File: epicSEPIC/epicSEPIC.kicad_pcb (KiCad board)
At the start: 2 copper layers, 24 x 27.4 mm, 12 parts, among them J1 Screw_Terminal_01x02, J2 Screw_Terminal_01x02, Q1 ISZ230N10NM6, U1 1EDN7550U

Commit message: PCB prototipo mejorado
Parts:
- added C4: 0.22u, Capacitor_SMD:C_0603_1608Metric, B.Cu at (165.0, 129.8)
- added C5: 0.1u, Capacitor_SMD:C_0603_1608Metric, B.Cu at (165.0, 126.3)
- added U2: LM7815, Package_TO_SOT_SMD:SOT-223-3_TabPin2, B.Cu at (171.0, 128.0)
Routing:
- net input: track 0.00 -> 17.4 mm, vias 0 -> 4
- net /S_Diodo: track 4.34 -> 0.00 mm
- net VDD: track 0.00 -> 2.93 mm, vias 0 -> 3
- added copper zone on F.Cu, net /S_Diodo
- added copper zone on B.Cu, net VDD
- added copper zone on F.Cu, net VDD
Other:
- board size 24 x 27.4 mm -> 28 x 28 mm

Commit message: PCB Final en proceso, encontré el inductor
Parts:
- added L1: 1.8m, footprints:SRF1280680M, F.Cu at (183.5, 113.2)
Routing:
- added copper zone on B.Cu, net input
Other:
- board outline removed

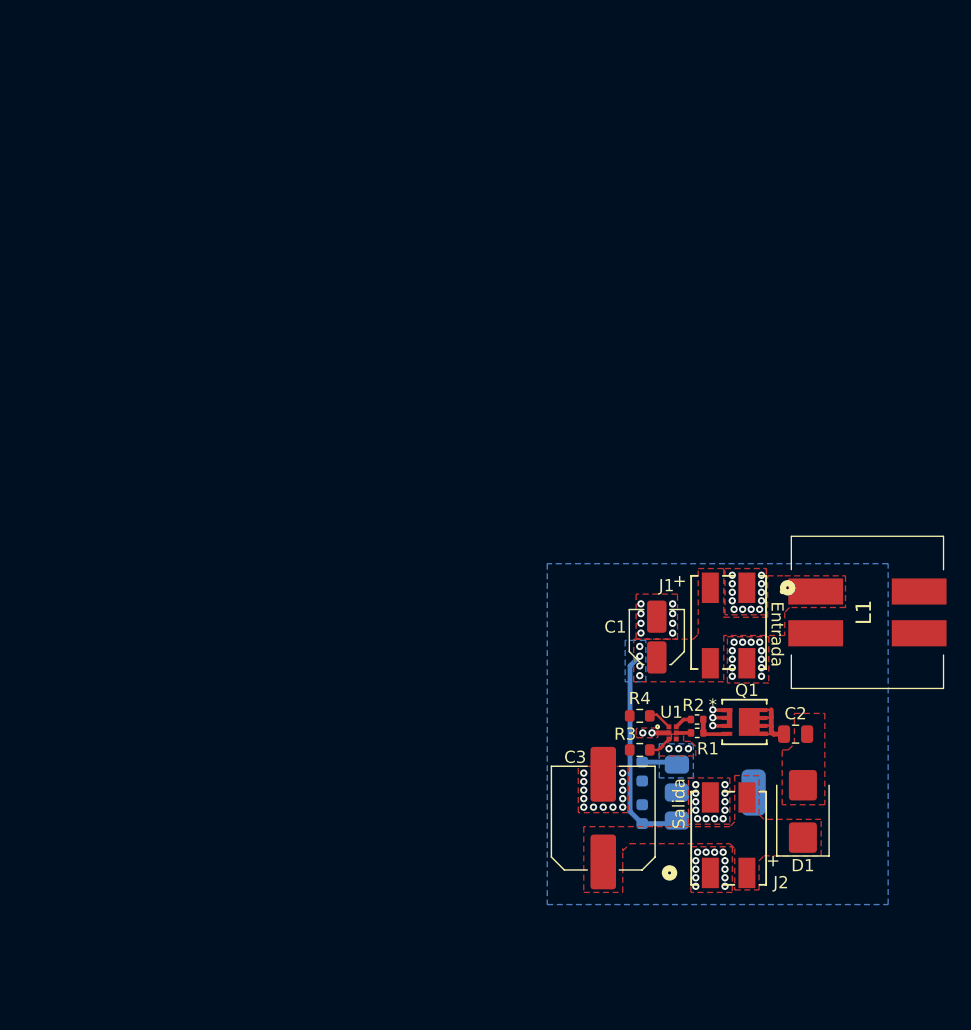
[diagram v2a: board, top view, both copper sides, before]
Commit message: Agregar repo submodulo para informe
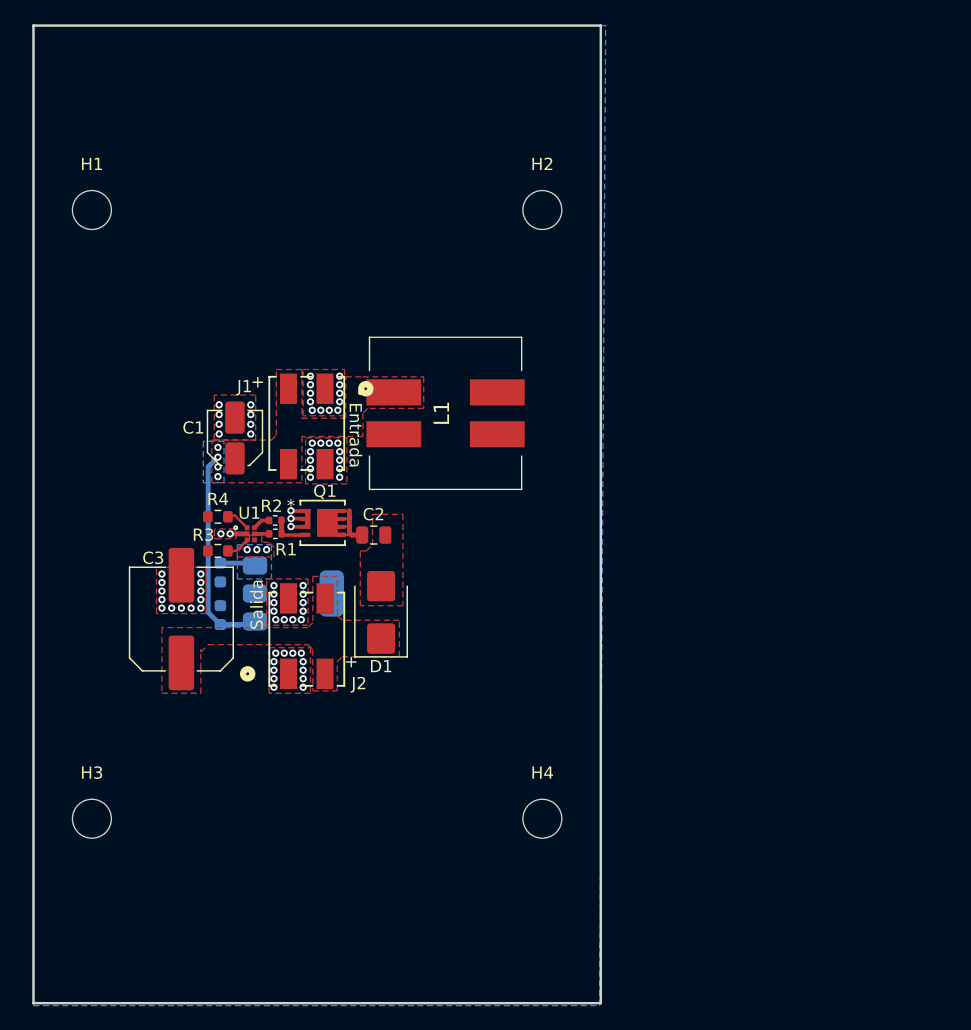
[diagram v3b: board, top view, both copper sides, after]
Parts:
- added H1: MountingHole, MountingHole:MountingHole_3.2mm_M3_ISO14580, F.Cu at (119.8, 80.2)
- added H2: MountingHole, MountingHole:MountingHole_3.2mm_M3_ISO14580, F.Cu at (156.8, 80.2)
- added H3: MountingHole, MountingHole:MountingHole_3.2mm_M3_ISO14580, F.Cu at (119.8, 130.2)
- added H4: MountingHole, MountingHole:MountingHole_3.2mm_M3_ISO14580, F.Cu at (156.8, 130.2)
- moved C2 38.3 mm to (142.9, 106.8)
- moved C4 38.3 mm to (130.3, 113.4)
- moved C5 38.3 mm to (130.3, 109.9)
- moved J1 38.3 mm to (137.4, 97.7)
- moved L1 38.3 mm to (148.8, 96.8)
- moved Q1 38.3 mm to (138.8, 105.8)
- moved R1 38.3 mm to (134.9, 106.8)
- moved R4 38.3 mm to (130.2, 105.3)
- moved U1 38.3 mm to (132.8, 106.8)
- moved C3 38.3 mm to (127.2, 113.8)
- moved J2 38.3 mm to (137.5, 115.4)
- moved R3 38.3 mm to (130.2, 108.2)
- moved U2 38.3 mm to (136.3, 111.7)
- moved D1 38.3 mm to (143.6, 113.2)
- moved C1 38.3 mm to (131.6, 98.9)
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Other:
- board outline added: 46.6 x 80.3 mm

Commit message: Diseño de PCB final
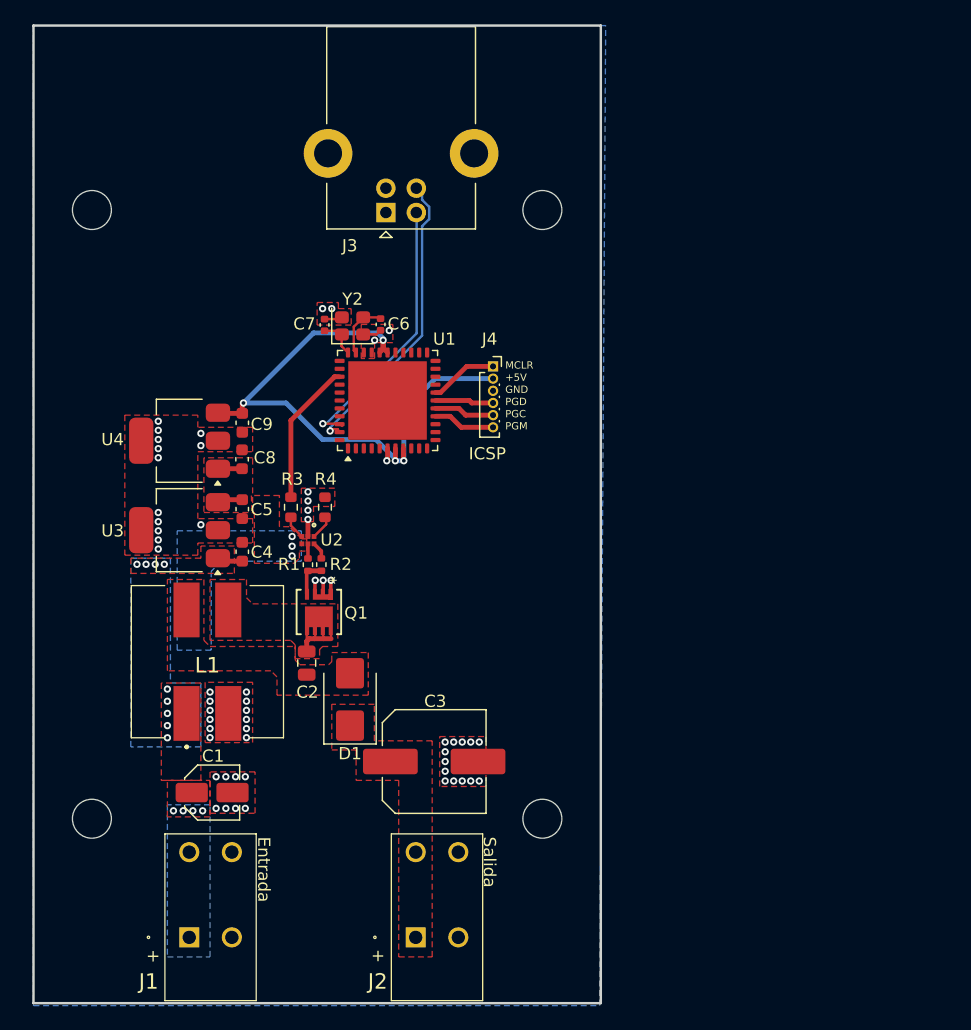
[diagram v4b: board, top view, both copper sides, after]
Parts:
- added C6: 20p, Capacitor_SMD:C_0402_1005Metric, F.Cu at (143.5, 89.6)
- added C7: 20p, Capacitor_SMD:C_0402_1005Metric, F.Cu at (138.9, 89.6)
- added C8: 0.22u, Capacitor_SMD:C_0603_1608Metric, F.Cu at (132.1, 100.6)
- added C9: 0.1u, Capacitor_SMD:C_0603_1608Metric, F.Cu at (132.2, 97.6)
- added J3: USB_B, Connector_USB:USB_B_Lumberg_2411_02_Horizontal, F.Cu at (143.9, 80.4)
- added J4: ICSP, Connector_PinSocket_1.00mm:PinSocket_1x06_P1.00mm_Vertical, F.Cu at (152.8, 93.0)
- added U1: PIC18F4550-IML, Package_DFN_QFN:QFN-44-1EP_8x8mm_P0.65mm_EP6.45x6.45mm, F.Cu at (144.1, 95.8)
- added U4: LM7805, Package_TO_SOT_SMD:SOT-223-3_TabPin2, F.Cu at (127.0, 99.1)
- added Y2: 20M, Crystal:Crystal_SMD_2520-4Pin_2.5x2.0mm, F.Cu at (141.2, 89.7)
- C4, C5: moved to F.Cu
- J1, J2: footprint footprints:CONN2_2059-322&slash_998-403_WAG -> footprints:1822752
- U3: renamed from U2; moved to F.Cu
- moved J1 43.3 mm to (127.8, 139.9), turned to 0 degrees
- moved C1 29.2 mm to (129.7, 128.0), turned to 0 degrees
- moved L1 28.3 mm to (129.3, 117.2), turned to 180 degrees
- moved J2 26.1 mm to (146.4, 139.9)
- moved C3 23.8 mm to (147.9, 125.5), turned to 0 degrees
- moved C2 11.9 mm to (137.4, 117.4), turned to -90 degrees
- moved U3 10.7 mm to (127.0, 106.5), turned to 180 degrees
- moved R4 8.83 mm to (138.9, 104.6), turned to -90 degrees
- moved D1 7.59 mm to (141.0, 120.3)
- moved Q1 7.32 mm to (138.4, 113.2), turned to -90 degrees
- moved R3 6.98 mm to (136.1, 104.6), turned to -90 degrees
- moved C4 5.51 mm to (132.1, 108.2)
- moved C5 5.51 mm to (132.1, 104.7)
- moved R2 5.24 mm to (138.6, 109.3), turned to -90 degrees
- moved U2 4.72 mm to (137.5, 107.3), turned to -90 degrees
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- renumbered U1 to U2
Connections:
- net VDD renamed +15V
- J1 pad 1: GND -> input
- J2 pad 1: GND -> output
- R4 pad 1: in- -> GND
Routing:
- net +5V: track 0.00 -> 49.2 mm, vias 0 -> 4
- net D-: track 0.00 -> 25.9 mm, vias 0 -> 1
- net D+: track 0.00 -> 24.6 mm, vias 0 -> 1
- net input: track 17.4 -> 2.10 mm, vias 4 -> 13
- net in+: track 0.00 -> 11.8 mm
- net MCLR: track 0.00 -> 5.62 mm
- net PGM: track 0.00 -> 5.10 mm
- net PGC: track 0.00 -> 4.96 mm
- net PGD: track 0.00 -> 4.81 mm
- net /OSC-: track 0.00 -> 4.75 mm
- net GND: track 4.88 -> 8.97 mm, vias 74 -> 58
- net /OSC+: track 0.00 -> 3.26 mm
- net +15V: track 2.93 -> 4.07 mm
- added copper zone on F.Cu, net /S_Drain
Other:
- board text added: "+5V"
- board text added: "GND"
- board text added: "ICSP"
- board text added: "MCLR"
- board text added: "PGC"
- board text added: "PGD"
- board text added: "PGM"

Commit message: PCB final
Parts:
- removed Y2: 20M, Crystal:Crystal_SMD_2520-4Pin_2.5x2.0mm
- added C11: 1u, Capacitor_SMD:C_0805_2012Metric, F.Cu at (144.2, 102.2)
- added C12: 0.1u, Capacitor_SMD:C_0805_2012Metric, F.Cu at (134.8, 102.0)
- added C13: 0.1u, Capacitor_SMD:C_0805_2012Metric, F.Cu at (144.2, 104.2)
- added C14: 10n, Capacitor_SMD:C_0603_1608Metric, F.Cu at (134.8, 100.2)
- added C15: 10n, Capacitor_SMD:C_0603_1608Metric, F.Cu at (145.2, 89.5)
- added C16: 1n, Capacitor_SMD:C_0402_1005Metric, F.Cu at (136.2, 109.2)
- added C17: 1n, Capacitor_SMD:C_0402_1005Metric, F.Cu at (150.8, 94.5)
- added Y1: 20M, Crystal:Crystal_SMD_2520-4Pin_2.5x2.0mm, F.Cu at (141.4, 89.7)
- C1: footprint Capacitor_SMD:C_Elec_4x5.8 -> Capacitor_SMD:CP_Elec_8x10
- C2: value 2.2u -> 0.68u; footprint Capacitor_SMD:C_0805_2012Metric -> Capacitor_SMD:C_1206_3216Metric
- C3: value C -> 100u; footprint Capacitor_SMD:C_Elec_8x10.2 -> Capacitor_SMD:CP_Elec_10x12.5
- C4: value 0.22u -> 20p; footprint Capacitor_SMD:C_0603_1608Metric -> Capacitor_SMD:C_0402_1005Metric
- C5: value 0.1u -> 20p; footprint Capacitor_SMD:C_0603_1608Metric -> Capacitor_SMD:C_0402_1005Metric
- C6: value 20p -> 0.22u; footprint Capacitor_SMD:C_0402_1005Metric -> Capacitor_SMD:C_0603_1608Metric
- C7: value 20p -> 0.1u; footprint Capacitor_SMD:C_0402_1005Metric -> Capacitor_SMD:C_0603_1608Metric
- J1: value Screw_Terminal_01x02 -> Entrada 24V
- J2: renamed from J3; value USB_B -> USB Tipo B
- J3: renamed from J2; value Screw_Terminal_01x02 -> Salida 12-48V
- L1: value 1.8m -> 1.35m
- R1, R2: value R -> 51k; footprint Resistor_SMD:R_0402_1005Metric -> Resistor_SMD:R_0603_1608Metric
- R3, R4: value 51k -> R; footprint Resistor_SMD:R_0603_1608Metric -> Resistor_SMD:R_0402_1005Metric
- moved C6 21.6 mm to (132.2, 108.0)
- moved C4 19.9 mm to (139.0, 89.5)
- moved C5 19.1 mm to (143.8, 89.5), turned to 90 degrees
- moved C7 16.8 mm to (132.2, 105.0), turned to -90 degrees
- moved C1 8.75 mm to (138.3, 129.4), turned to 90 degrees
- moved R3 4.89 mm to (137.5, 109.3)
- moved C3 4.81 mm to (150.2, 121.2)
- moved R1 4.79 mm to (136.2, 104.7)
- moved R4 4.70 mm to (138.8, 109.3)
- moved R2 4.61 mm to (139.0, 104.7)
- moved J3 0.70 mm to (147.1, 139.8)
- moved J1 0.53 mm to (127.3, 139.8)
- moved C2 0.35 mm to (137.6, 117.7)
- moved U4 0.18 mm to (126.8, 99.0)
- moved C9 0.16 mm to (132.2, 97.5)
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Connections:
- net /S_Diodo renamed /Potencia/S_Diodo
- net /S_Drain renamed /Potencia/S_Drain
- net D+ renamed /Control/D+
- net D- renamed /Control/D-
- net output renamed /Potencia/Vout
- C1 pad 1: input -> /Potencia/Vin
- C4 pad 1: input -> /Control/OSC2
- C5 pad 1: +15V -> GND
- C5 pad 2: GND -> /Control/OSC1
- C6 pad 1: GND -> /Potencia/Vin
- C6 pad 2: /OSC- -> GND
- C7 pad 1: /OSC+ -> +15V
- J1 pad 1: input -> /Potencia/Vin
- J1 pad 2: input -> /Potencia/Vin
- L1 pad 1: input -> /Potencia/Vin
- Q1 pad 4: PWM -> /Control/PWM_gate
- R1 pad 1: Net-(U2-OUT_SRC) -> /Control/PWM
- R1 pad 2: PWM -> Net-(U2-IN+)
- R2 pad 1: Net-(U2-OUT_SNK) -> GND
- R2 pad 2: PWM -> Net-(U2-IN-)
- R3 pad 1: in+ -> Net-(U2-OUT_SRC)
- R3 pad 2: Net-(U2-IN+) -> /Control/PWM_gate
- R4 pad 1: GND -> Net-(U2-OUT_SNK)
- R4 pad 2: Net-(U2-IN-) -> /Control/PWM_gate
- U1 pad 32: /OSC- -> /Control/OSC1
- U1 pad 33: /OSC+ -> /Control/OSC2
- U1 pad 36: in+ -> /Control/PWM
- U1 pad 37: V_{USB} -> unconnected-(U1-VUSB-Pad37)
- U3 pad 1: input -> /Potencia/Vin
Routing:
- net in+: track 11.8 -> 0.00 mm
- net /Control/PWM: track 0.00 -> 11.8 mm
- net GND: track 8.97 -> 17.2 mm, vias 58 -> 61
- net +5V: track 49.2 -> 56.7 mm
- net /OSC-: track 4.75 -> 0.00 mm
- net /Control/OSC1: track 0.00 -> 4.75 mm
- net /OSC+: track 3.26 -> 0.00 mm
- net /Control/OSC2: track 0.00 -> 3.26 mm
- net PWM: track 3.06 -> 0.00 mm
- net /Control/PWM_gate: track 0.00 -> 3.06 mm
- net input: track 2.10 -> 0.00 mm, vias 13 -> 0
- net +15V: track 4.07 -> 1.98 mm
- net /Potencia/Vin: vias 0 -> 9
- added copper zone on B.Cu, net /Potencia/Vin
- added copper zone on F.Cu, net /Potencia/Vin
- removed copper zone on B.Cu, net input
- removed copper zone on F.Cu, net input

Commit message: Agregar datasheets
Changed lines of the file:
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@@
 		(tags "capacitor")
 		(property "Reference" "C17"
-			(at -0.25 1.25 90)
+			(at -1.5 0.36 180)
 			(layer "F.SilkS")
 			(effects
@@
 		(tags "QFN NoLead")
 		(property "Reference" "U1"
-			(at 0 -5.3 90)
-			(layer "F.SilkS")
-			(effects
+			(at 2.8125 -5.6 180)
+			(layer "F.SilkS")
+			(effects

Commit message: PCB Final con reguladores
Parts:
- added C10: 100n, Capacitor_SMD:C_0402_1005Metric, F.Cu at (157.5, 112.4)
- added C11: 33u, Capacitor_SMD:C_0805_2012Metric, F.Cu at (154.7, 99.3)
- added L2: 15u, Inductor_SMD_Wurth:L_Wurth_WE-LHMI-7050, F.Cu at (127.1, 100.0)
- added L3: 13u, Inductor_SMD_Wurth:L_Wurth_WE-PDF-1064, F.Cu at (152.8, 105.9)
- added R5: 100k, Resistor_SMD:R_0402_1005Metric, F.Cu at (132.3, 107.4)
- added R6: 4.12k, Resistor_SMD:R_0402_1005Metric, F.Cu at (132.3, 109.7)
- added R7: 100k, Resistor_SMD:R_0402_1005Metric, F.Cu at (158.0, 114.8)
- added R8: 13.7k, Resistor_SMD:R_0402_1005Metric, F.Cu at (158.0, 117.1)
- C6: value 0.22u -> 470n
- C7: value 0.1u -> 100n; footprint Capacitor_SMD:C_0603_1608Metric -> Capacitor_SMD:C_0402_1005Metric
- C8: value 0.22u -> 15u; footprint Capacitor_SMD:C_0603_1608Metric -> Capacitor_SMD:C_0805_2012Metric
- C9: value 0.1u -> 470n
- D1: value D_Schottky -> SK52
- R3, R4: value R -> 2
- U3: value LM7815 -> TPS54308; footprint Package_TO_SOT_SMD:SOT-223-3_TabPin2 -> Package_TO_SOT_SMD:SOT-23-6
- U4: value LM7805 -> TPS54308; footprint Package_TO_SOT_SMD:SOT-223-3_TabPin2 -> Package_TO_SOT_SMD:SOT-23-6
- moved U4 30.4 mm to (153.4, 113.8), turned to 0 degrees
- moved C9 23.8 mm to (149.6, 113.8), turned to 90 degrees
- moved C15 18.1 mm to (136.5, 87.9), turned to 90 degrees
- moved C13 15.5 mm to (138.5, 87.9), turned to 90 degrees
- moved C4 14.1 mm to (151.3, 82.6), turned to 0 degrees
- moved Y1 10.8 mm to (151.1, 85.0), turned to -90 degrees
- moved C6 8.49 mm to (123.9, 106.4)
- moved U1 8.16 mm to (145.0, 87.7), turned to 0 degrees
- moved C5 7.83 mm to (151.3, 87.4), turned to 0 degrees
- moved C8 6.96 mm to (128.9, 94.4), turned to 180 degrees
- moved C17 6.08 mm to (151.3, 88.9), turned to 0 degrees
- moved J4 5.98 mm to (147.8, 96.4), turned to -90 degrees
- moved C18 4.45 mm to (146.3, 94.4), turned to 180 degrees
- moved U3 0.81 mm to (127.7, 106.5), turned to 0 degrees
- moved C7 0.45 mm to (131.8, 105.0), turned to 90 degrees
- renumbered C11 to C13, C13 to C15, C15 to C17, C17 to C18
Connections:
- C7 pad 1: +15V -> Net-(U3-BOOT)
- C7 pad 2: GND -> Net-(U3-SW)
- C8 pad 1: +15V -> GND
- C8 pad 2: GND -> +15V
- C9 pad 1: +5V -> /Potencia/Vin
- U3 pad 1: /Potencia/Vin -> GND
- U3 pad 2: GND -> Net-(U3-SW)
- U3 pad 3: +15V -> /Potencia/Vin
- U4 pad 1: +15V -> GND
- U4 pad 2: GND -> Net-(U4-SW)
- U4 pad 3: +5V -> /Potencia/Vin
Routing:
- net +5V: track 56.7 -> 34.2 mm, vias 4 -> 0
- net /Control/PWM: track 11.8 -> 26.1 mm, vias 0 -> 2
- net /Control/D-: track 25.9 -> 12.2 mm, vias 1 -> 0
- net /Control/D+: track 24.6 -> 12.2 mm, vias 1 -> 0
- net +15V: track 1.98 -> 13.9 mm
- net Net-(U4-FB): track 0.00 -> 5.67 mm
- net Net-(U3-FB): track 0.00 -> 5.63 mm
- net Net-(U3-SW): track 0.00 -> 5.45 mm
- net Net-(U4-BOOT): track 0.00 -> 3.01 mm
- net Net-(U3-BOOT): track 0.00 -> 3.01 mm
- net GND: track 17.2 -> 15.4 mm, vias 61 -> 198
- net /Potencia/Vin: vias 9 -> 14
- added copper zone on F.Cu, net +5V
- added copper zone on F.Cu, net Net-(U3-SW)
- added copper zone on F.Cu, net Net-(U4-SW)
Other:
- outline, holes or cut-outs redrawn
- board text added: "Taller de Sistemas Electrónicos"
